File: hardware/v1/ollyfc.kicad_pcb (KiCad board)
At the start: 4 copper layers, 50 x 95 mm, 98 parts, among them J1 Conn_01x06, J10 Conn_01x03, J11 Conn_01x03, J13 Conn_01x05, J2 Conn_01x02, J3 Conn_01x03, J4 USB_C_Receptacle_USB2.0, J5 Conn_02x05_Odd_Even, J6 Conn_01x03, J7 Conn_01x03, J8 Conn_Coaxial, J9 Conn_01x03, Q1 AO3401A, Q2 MMBT3904, Q3 MMBT3904, Q4 MMBT3904, SW1 ACT/PASS, SW2 SW_Push, SW3 SW_Push, SW4 MODE1, SW5 MODE1, U1 AMS1117-3.3, U10 SRV05-4, U2 PCA9685BS, U3 STM32F411RETx, U4 LIS3MDL, U5 BMI088, U6 W25Q128JVS, U7 BMP388, U8 NEO-M8N, U9 TPS2113APW, Y1 X322516MLB4SI

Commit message: Route another?
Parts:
- removed R17: 5K1, Resistor_SMD:R_0402_1005Metric
- removed SW1: ACT/PASS, Button_Switch_SMD:SW_SPDT_PCM12
- added H6: MountingHole, MountingHole:MountingHole_3.2mm_M3, F.Cu at (15.2, 19.5)
- added J12: Conn_01x04, Connector_PinHeader_2.54mm:PinHeader_1x05_P2.54mm_Vertical, F.Cu at (-7.66, 16.8)
- added J14: Conn_01x04, Connector_PinHeader_2.54mm:PinHeader_1x04_P2.54mm_Vertical, F.Cu at (13.8, -14.7)
- added J15: Conn_01x04, Connector_PinHeader_2.54mm:PinHeader_1x04_P2.54mm_Vertical, F.Cu at (2.40, 20.8)
- added JP1: Jumper_2_Open, Connector_PinHeader_2.54mm:PinHeader_1x02_P2.54mm_Vertical, F.Cu at (9.25, -37.0)
- added R1: 5K1, Resistor_SMD:R_0402_1005Metric, F.Cu at (5.60, -17.2)
- J13: value Conn_01x05 -> Conn_01x04; footprint Connector_PinHeader_2.54mm:PinHeader_1x05_P2.54mm_Vertical -> Connector_PinHeader_2.54mm:PinHeader_1x04_P2.54mm_Vertical
- moved H1 99.0 mm to (15.2, -37.5)
- moved R12 83.5 mm to (11.5, -16.0), turned to 90 degrees
- moved H4 80.1 mm to (15.2, 50.0)
- moved BT1 71.4 mm to (-8.60, -23.8), turned to -90 degrees
- moved R6 68.0 mm to (18.2, -1.75), turned to 90 degrees
- moved R7 67.3 mm to (9.75, 7.00), turned to 90 degrees
- moved R10 64.3 mm to (18.2, 0.51), turned to -90 degrees
- moved SW5 63.5 mm to (18.1, -9.70), turned to 90 degrees
- moved D1 60.8 mm to (19.2, -3.75), turned to 180 degrees
- moved D3 58.1 mm to (19.2, 2.50), turned to 180 degrees
- moved J3 47.2 mm to (-17.2, 31.3), turned to 0 degrees
- moved H5 43.9 mm to (-15.2, 19.5)
- moved J6 42.0 mm to (-17.2, 37.0), turned to 0 degrees
- moved J13 40.3 mm to (-17.5, -8.79)
- moved R26 39.9 mm to (-0.99, 37.5)
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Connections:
- net SWDCLK renamed JTCK_SWCLK
- net SWDIO renamed JTMS_SWDIO
- net SWO renamed JTDO_SWO
- BZ1 pad N: (no net) -> Net-(BZ1-+)
- BZ1 pad P: (no net) -> 5VIN
- C26 pad 1: Net-(C26-Pad1) -> Net-(JP1-B)
- J5 pad 10: NRST -> JTRST
- J5 pad 8: unconnected-(J5-Pin_8-Pad8) -> JTDI
- L1 pad 1: Net-(C26-Pad1) -> Net-(JP1-A)
- Q3 pad 3: USART6_RX -> USART1_RX
- R12 pad 2: I2C3_SCL -> I2C1_SCL
- R19 pad 1: Net-(SW1-C) -> Net-(U8-VCC_RF)
- R19 pad 2: Net-(C26-Pad1) -> Net-(JP1-B)
- R2 pad 1: USART6_TX -> USART1_TX
- R5 pad 1: USART6_RX -> USART1_RX
- R8 pad 2: I2C2_SCL -> I2C2_SDA
- R9 pad 2: I2C2_SDA -> I2C2_SCL
- U2 pad 10: STATUS_B -> unconnected-(U2-LED7-Pad10)
- U2 pad 15: unconnected-(U2-LED11-Pad15) -> /IO/SERVO_CH4
- U2 pad 16: unconnected-(U2-LED12-Pad16) -> /IO/SERVO_CH5
- U2 pad 17: /IO/SERVO_CH4 -> /IO/SERVO_CH6
- U2 pad 18: /IO/SERVO_CH5 -> STATUS_A
- U2 pad 19: /IO/SERVO_CH6 -> STATUS_B
- U2 pad 23: I2C3_SCL -> I2C2_SCL
- U2 pad 24: I2C3_SDA -> I2C2_SDA
- U2 pad 9: STATUS_A -> unconnected-(U2-LED6-Pad9)
- U3 pad 10: SPI2_MOSI -> MODE1
- U3 pad 11: SPI2_MISO -> unconnected-(U3-PC3-Pad11)
- U3 pad 2: LED1 -> MAG_INT
- U3 pad 20: USART2_CK -> FMEM_CS
- U3 pad 21: PWR_STATE -> SPI1_SCK
- U3 pad 22: GYRO_INT3 -> SPI1_MISO
- U3 pad 23: CSB_GYRO -> SPI1_MOSI
- U3 pad 24: GYRO_INT4 -> unconnected-(U3-PC4-Pad24)
- U3 pad 25: CSB_ACCEL -> unconnected-(U3-PC5-Pad25)
- U3 pad 26: ACCEL_INT1 -> FMEM_HOLD
- U3 pad 27: GNSS_TIMEP -> PRES_INT
- U3 pad 28: GNSS_INT -> unconnected-(U3-PB2-Pad28)
- U3 pad 3: LED2 -> ACCEL_INT2
- U3 pad 34: SPI2_SCK -> unconnected-(U3-PB13-Pad34)
- U3 pad 35: MAG_CS -> LED2
- U3 pad 36: MAG_DRDY -> unconnected-(U3-PB15-Pad36)
- U3 pad 37: USART6_TX -> PWR_STATE
- U3 pad 38: USART6_RX -> LED1
- U3 pad 39: MAG_INT -> MODE2
- U3 pad 4: unconnected-(U3-PC15-Pad4) -> ACCEL_INT1
- U3 pad 40: I2C3_SDA -> unconnected-(U3-PC9-Pad40)
- U3 pad 41: I2C3_SCL -> unconnected-(U3-PA8-Pad41)
- U3 pad 42: BUZZER -> USART1_TX
- U3 pad 43: GNSS_CS -> USART1_RX
- U3 pad 50: FMEM_CS -> JTDI
- U3 pad 51: SPI1_SCK -> GNSS_TIMEP
- U3 pad 52: SPI1_MISO -> GNSS_INT
- U3 pad 53: SPI1_MOSI -> GNSS_RESET
- U3 pad 56: FMEM_HOLD -> JTRST
- U3 pad 57: unconnected-(U3-PB5-Pad57) -> GYRO_INT3
- U3 pad 58: MODE1 -> I2C1_SCL
- U3 pad 59: MODE2 -> I2C1_SDA
- U3 pad 61: ACCEL_INT2 -> GYRO_INT4
- U3 pad 8: PWR_STATE -> unconnected-(U3-PC0-Pad8)
- U3 pad 9: PRES_INT -> MAG_DRDY
- U4 pad 1: SPI2_SCK -> I2C1_SCL
- U4 pad 10: MAG_CS -> +3V3
- U4 pad 11: SPI2_MOSI -> I2C1_SDA
- U4 pad 9: SPI2_MISO -> GND
- U5 pad 10: SPI2_MISO -> GND
- U5 pad 14: CSB_ACCEL -> +3V3
- U5 pad 15: SPI2_MISO -> GND
- U5 pad 2: unconnected-(U5-NC-Pad2) -> GND
- U5 pad 5: CSB_GYRO -> unconnected-(U5-CSB2-Pad5)
- U5 pad 7: GND -> +3V3
- U5 pad 8: SPI2_SCK -> I2C1_SCL
- U5 pad 9: SPI2_MOSI -> I2C1_SDA
- U8 pad 14: LNA_EN -> unconnected-(U8-LNA_EN-Pad14)
- U8 pad 18: GNSS_CS -> I2C1_SDA
- U8 pad 19: SPI2_SCK -> I2C1_SCL
- U8 pad 2: GND -> unconnected-(U8-D_SEL-Pad2)
- U8 pad 20: SPI2_MISO -> unconnected-(U8-TXD/SPI_MISO-Pad20)
- U8 pad 21: SPI2_MOSI -> unconnected-(U8-RXD/SPI_MOSI-Pad21)
- U8 pad 9: Net-(SW1-B) -> Net-(U8-VCC_RF)
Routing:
- net SPI2_MISO: track 86.3 -> 0.00 mm, vias 6 -> 0
- net SPI2_MOSI: track 66.5 -> 0.00 mm, vias 3 -> 0
- net SPI2_SCK: track 65.2 -> 0.00 mm, vias 5 -> 0
- net I2C1_SDA: track 0.00 -> 64.0 mm, vias 0 -> 3
- net VBUS: track 74.9 -> 14.9 mm, vias 3 -> 6
- net I2C1_SCL: track 0.00 -> 57.7 mm, vias 0 -> 2
- net I2C2_SCL: track 7.13 -> 63.4 mm, vias 0 -> 2
- net USART2_CK: track 48.4 -> 0.00 mm, vias 1 -> 0
- net VIN_EXT: track 43.0 -> 0.00 mm
- net VBAT: track 3.54 -> 43.0 mm, vias 0 -> 2
- net MAG_CS: track 35.3 -> 0.00 mm, vias 4 -> 0
- net I2C2_SDA: track 27.6 -> 62.6 mm, vias 2 -> 1
- net Net-(D4-A): track 35.8 -> 1.62 mm, vias 2 -> 0
- net GNSS_RESET: track 1.60 -> 34.4 mm, vias 1 -> 2
- net USART1_RX: track 0.00 -> 31.9 mm
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- added copper zone on In2.Cu, net +3V3
- added copper zone on In2.Cu, net VBUS
- added copper zone on F.Cu, net VIN_EXT
- removed copper zone on F.Cu, net VIN
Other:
- board size 50 x 95 mm -> 42.5 x 99.5 mm
- board text added: "EXT ANT."
- board text added: "I2C1"
- board text removed: "P A"

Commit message: v2 PCB design
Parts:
- removed BT1: Battery_Cell, Battery:BatteryHolder_Keystone_3002_1x2032
- removed H6: MountingHole, MountingHole:MountingHole_3.2mm_M3
- removed J15: Conn_01x04, Connector_PinHeader_2.54mm:PinHeader_1x04_P2.54mm_Vertical
- BZ1: moved to B.Cu
- J13: footprint Connector_PinHeader_2.54mm:PinHeader_1x04_P2.54mm_Vertical -> Connector_PinHeader_2.54mm:PinHeader_1x08_P2.54mm_Vertical
- moved SW4 37.3 mm to (16.5, -29.0), turned to 90 degrees
- moved D4 36.8 mm to (-9.11, 21.2), turned to 0 degrees
- moved C15 35.2 mm to (-8.25, -20.5), turned to 90 degrees
- moved R8 34.7 mm to (2.75, -10.5), turned to -90 degrees
- moved D2 34.7 mm to (-3.00, 51.2), turned to 0 degrees
- moved U7 34.0 mm to (-6.24, -20.8), turned to 90 degrees
- moved R13 33.2 mm to (-5.86, 21.2), turned to 180 degrees
- moved C14 32.1 mm to (-7.25, -18.5), turned to 0 degrees
- moved R16 31.8 mm to (-2.75, 49.8), turned to 180 degrees
- moved J4 30.6 mm to (16.1, 40.9)
- moved H1 30.5 mm to (-15.2, -37.5)
- moved H2 30.5 mm to (15.2, -37.5)
- moved H5 30.5 mm to (15.2, 19.5)
- moved R7 30.4 mm to (9.25, 37.4)
- moved SW3 29.3 mm to (11.5, 9.75), turned to 0 degrees
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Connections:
- J13 pad 1: USART2_CTS -> GND
- J13 pad 2: USART2_RTS -> +3V3
- J13 pad 3: USART2_TX -> I2C2_SCL
- J13 pad 4: USART2_RX -> I2C2_SDA
- U3 pad 10: MODE1 -> unconnected-(U3-PC2-Pad10)
- U3 pad 2: MAG_INT -> unconnected-(U3-PC13-Pad2)
- U3 pad 24: unconnected-(U3-PC4-Pad24) -> MAG_INT
- U3 pad 27: PRES_INT -> MODE1
- U3 pad 28: unconnected-(U3-PB2-Pad28) -> MODE2
- U3 pad 3: ACCEL_INT2 -> ACCEL_INT1
- U3 pad 36: unconnected-(U3-PB15-Pad36) -> BUZZER
- U3 pad 39: MODE2 -> unconnected-(U3-PC8-Pad39)
- U3 pad 4: ACCEL_INT1 -> ACCEL_INT2
- U3 pad 41: unconnected-(U3-PA8-Pad41) -> GNSS_SAFEBOOT
- U3 pad 51: GNSS_TIMEP -> GNSS_RESET
- U3 pad 53: GNSS_RESET -> GNSS_TIMEP
- U3 pad 8: unconnected-(U3-PC0-Pad8) -> MAG_DRDY
- U3 pad 9: MAG_DRDY -> PRES_INT
- U7 pad 2: I2C2_SCL -> I2C1_SCL
- U7 pad 4: I2C2_SDA -> I2C1_SDA
- U8 pad 18: I2C1_SDA -> I2C2_SDA
- U8 pad 19: I2C1_SCL -> I2C2_SCL
- U8 pad 22: VBAT -> +3V3
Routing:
- net VIN_EXT: track 0.00 -> 49.3 mm
- net GNSS_SAFEBOOT: track 0.00 -> 47.3 mm, vias 0 -> 2
- net VBAT: track 43.0 -> 0.00 mm, vias 2 -> 0
- net GND: track 122.3 -> 156.2 mm, vias 86 -> 79
- net VBUS: track 14.9 -> 43.8 mm, vias 6 -> 5
- net I2C2_SDA: track 62.6 -> 90.1 mm, vias 1 -> 4
- net USART1_RX: track 31.9 -> 4.68 mm
- net /SBUS_OUT: track 10.3 -> 37.1 mm
- net I2C2_SCL: track 63.4 -> 88.7 mm, vias 2 -> 4
- net USBD-: track 22.0 -> 46.9 mm
- net /S_PORT: track 13.8 -> 37.6 mm
- net USBD+: track 22.1 -> 45.5 mm
- net I2C1_SDA: track 64.0 -> 41.9 mm, vias 3 -> 0
- net PWR_STATE: track 27.8 -> 49.4 mm, vias 2 -> 0
- net MODE1: track 24.6 -> 46.1 mm
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- added copper zone on F.Cu, net VIN
- removed copper zone on F.Cu, net 5VIN
- removed copper zone on In2.Cu, net VBUS
- removed copper zone on F.Cu, net VIN_EXT
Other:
- board size 42.5 x 99.5 mm -> 40.5 x 97.5 mm
- board text added: "SPI1"
- board text added: "ch1"
- board text added: "ch2"
- board text added: "ch3"
- board text added: "ch4"
- board text added: "ch5"
- board text added: "ch6"
- board text removed: "EXT ANT."
- board text removed: "I2C1"

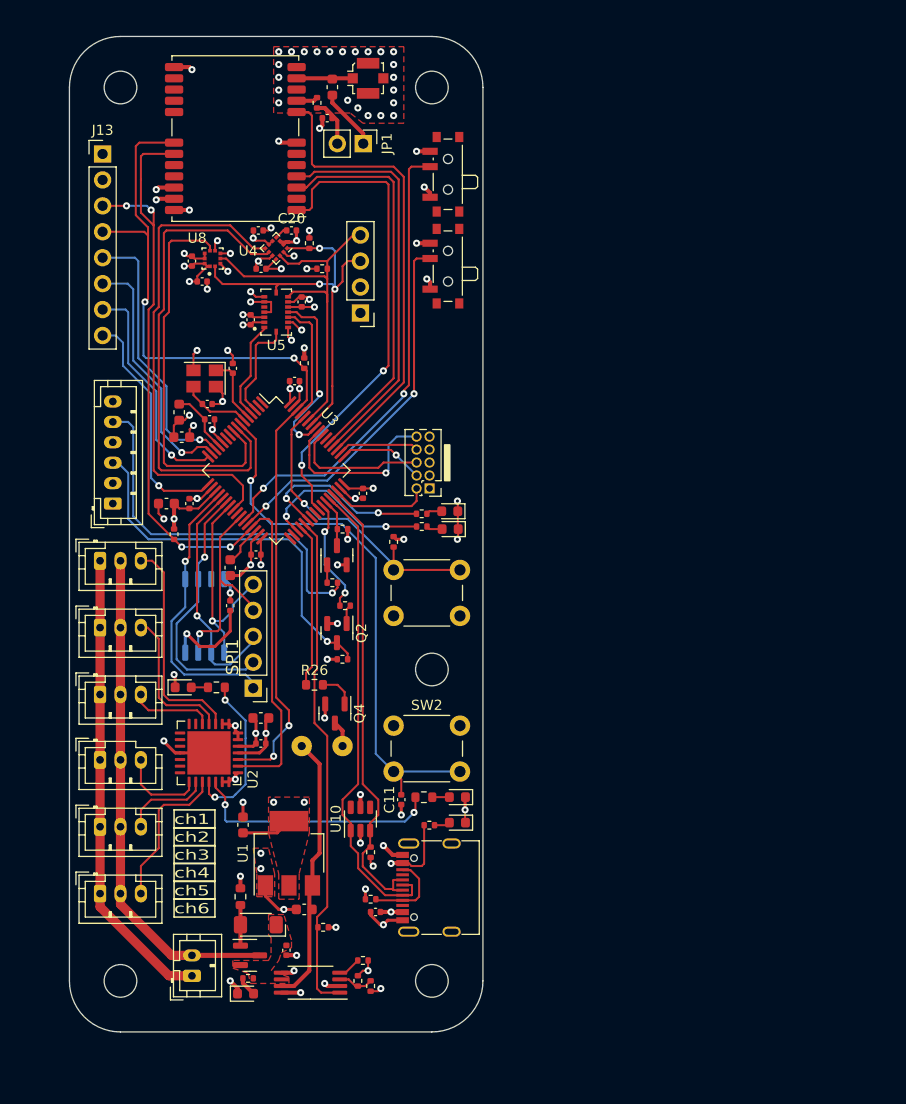
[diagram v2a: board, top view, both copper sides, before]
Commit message: JLC part footprints
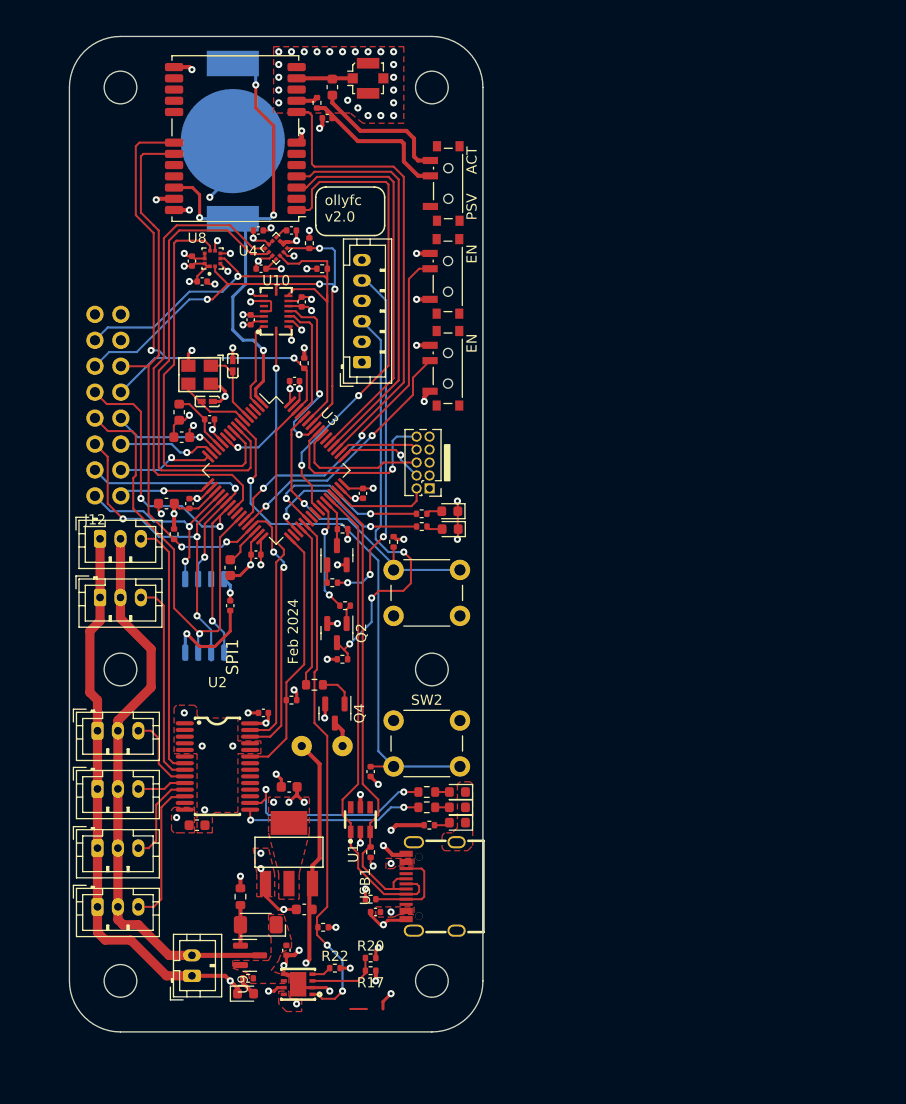
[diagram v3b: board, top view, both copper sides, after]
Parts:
- removed J14: Conn_01x04, Connector_PinHeader_2.54mm:PinHeader_1x04_P2.54mm_Vertical
- removed J4: USB_C_Receptacle_USB2.0, Connector_USB:USB_C_Receptacle_G-Switch_GT-USB-7010ASV
- removed JP1: Jumper_2_Open, Connector_PinHeader_2.54mm:PinHeader_1x02_P2.54mm_Vertical
- removed R24: 1K5, Resistor_SMD:R_0402_1005Metric
- removed U5: BMI088, ollyfc:PQFN50P450X300X100-16N
- removed Y1: X322516MLB4SI, Crystal:Crystal_SMD_SeikoEpson_TSX3225-4Pin_3.2x2.5mm
- added BT1: Battery_Cell, Battery:BatteryHolder_LINX_BAT-HLD-012-SMT, B.Cu at (-4.25, -32.2)
- added D8: SRV05-4_C7420376, ofc_sym:SOT-23-6_L2.9-W1.6-P0.95-LS2.8-BL-1, F.Cu at (8.25, 34.2)
- added H6: MountingHole, MountingHole:MountingHole_3.2mm_M3, F.Cu at (-15.2, 19.5)
- added R17: 1K5, Resistor_SMD:R_0402_1005Metric, F.Cu at (9.25, 49.0)
- added R20: 1K5, Resistor_SMD:R_0402_1005Metric, F.Cu at (9.25, 47.8)
- added SW6: MODE1, Button_Switch_SMD:SW_SPDT_PCM12, F.Cu at (16.5, -28.1)
- added USB1: USB-TYPE-C-018, ofc_sym:USB-C_SMD-TYPE-C-31-M-12, F.Cu at (15.2, 40.8)
- added X1: X322516MLB4SI, ofc_sym:OSC-SMD_4P-L3.2-W2.5-BL, F.Cu at (-7.50, -9.37)
- C10, C9: value 10pF -> 12pF; footprint Capacitor_SMD:C_0402_1005Metric -> ofc_sym:C0402
- J12: value Conn_01x04 -> Conn_01x08; footprint Connector_PinHeader_2.54mm:PinHeader_1x05_P2.54mm_Vertical -> Connector_PinHeader_2.54mm:PinHeader_1x08_P2.54mm_Vertical
- R23: value 1K5 -> 5K1
- U1: footprint Package_TO_SOT_SMD:SOT-223-3_TabPin2 -> ofc_sym:SOT-223-3_L6.5-W3.4-P2.30-LS7.0-BR
- U10: value SRV05-4 -> BMI088; footprint Package_TO_SOT_SMD:SOT-23-6 -> ofc_sym:LGA-16_L4.5-W3.0-P0.50-BL
- U2: value PCA9685BS -> PCA9685PW,118; footprint Package_DFN_QFN:QFN-28-1EP_6x6mm_P0.65mm_EP4.25x4.25mm -> ofc_sym:TSSOP-28_L9.7-W4.4-P0.65-LS6.4-TL
- U9: value TPS2113APW -> TPS2113ADRBR; footprint Package_SO:TSSOP-8_4.4x3mm_P0.65mm -> ofc_sym:SON-8_L3.0-W3.0-P0.65-LS3.0-BL-EP
- moved U10 50.4 mm to (0.00, -15.6), turned to 0 degrees
- moved D4 29.3 mm to (17.8, 33.0), turned to 180 degrees
- moved R23 29.1 mm to (1.50, 22.5), turned to 0 degrees
- moved J1 28.1 mm to (8.40, -10.6)
- moved J12 24.4 mm to (-17.8, 2.50)
- moved R13 23.7 mm to (14.8, 33.0), turned to 0 degrees
- moved J13 15.8 mm to (-15.2, -15.3)
- moved C18 12.2 mm to (-7.75, 34.8), turned to 0 degrees
- moved SW4 10.0 mm to (16.5, -19.0)
- moved SW5 10.0 mm to (16.5, -10.0)
- moved C19 5.86 mm to (1.27, 31.0), turned to 180 degrees
- moved C11 4.07 mm to (9.25, 29.5)
- moved J7 3.56 mm to (-17.5, 25.5)
- moved C17 3.01 mm to (-1.25, 23.8)
- moved J6 2.95 mm to (-17.3, 12.4)
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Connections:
- J13 pad 1: GND -> +3V3
- J13 pad 2: +3V3 -> unconnected-(J13-Pin_2-Pad2)
- R21 pad 1: Net-(J4-CC1) -> USBCC
- R23 pad 1: VBUS -> PWM_EN
- R23 pad 2: /Power/VSNS -> GND
- U10 pad 1: USBD- -> ACCEL_INT2
- U10 pad 3: USBD+ -> +3V3
- U10 pad 4: unconnected-(U10-IO3-Pad4) -> GND
- U10 pad 5: VBUS -> unconnected-(U10-CSB2-Pad5)
- U10 pad 6: unconnected-(U10-IO4-Pad6) -> GND
- U2 pad 10: unconnected-(U2-LED7-Pad10) -> /IO/SERVO_CH4
- U2 pad 11: GND -> /IO/SERVO_CH5
- U2 pad 12: unconnected-(U2-LED8-Pad12) -> /IO/SERVO_CH6
- U2 pad 14: unconnected-(U2-LED10-Pad14) -> +3V3
- U2 pad 15: /IO/SERVO_CH4 -> STATUS_A
- U2 pad 16: /IO/SERVO_CH5 -> STATUS_B
- U2 pad 17: /IO/SERVO_CH6 -> unconnected-(U2-LED10-Pad17)
- U2 pad 18: STATUS_A -> unconnected-(U2-LED11-Pad18)
- U2 pad 19: STATUS_B -> unconnected-(U2-LED12-Pad19)
- U2 pad 20: GND -> unconnected-(U2-LED13-Pad20)
- U2 pad 21: GND -> unconnected-(U2-LED14-Pad21)
- U2 pad 22: GND -> unconnected-(U2-LED15-Pad22)
- U2 pad 23: I2C2_SCL -> PWM_EN
- U2 pad 24: I2C2_SDA -> GND
- U2 pad 25: +3V3 -> GND
- U2 pad 26: GND -> I2C2_SCL
- U2 pad 27: GND -> I2C2_SDA
- U2 pad 28: GND -> +3V3
- U2 pad 3: /IO/SERVO_CH1 -> GND
- U2 pad 4: /IO/SERVO_CH2 -> GND
- U2 pad 5: /IO/SERVO_CH3 -> GND
- U2 pad 7: unconnected-(U2-LED4-Pad7) -> /IO/SERVO_CH1
- U2 pad 8: unconnected-(U2-LED5-Pad8) -> /IO/SERVO_CH2
- U2 pad 9: unconnected-(U2-LED6-Pad9) -> /IO/SERVO_CH3
- U3 pad 11: unconnected-(U3-PC3-Pad11) -> ACCEL_INT1
- U3 pad 2: unconnected-(U3-PC13-Pad2) -> ACCEL_INT2
- U3 pad 3: ACCEL_INT1 -> unconnected-(U3-PC14-Pad3)
- U3 pad 33: unconnected-(U3-PB12-Pad33) -> PWM_EN
- U3 pad 4: ACCEL_INT2 -> unconnected-(U3-PC15-Pad4)
- U8 pad 22: +3V3 -> VBAT
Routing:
- net VBAT: track 0.00 -> 51.1 mm, vias 0 -> 4
- net PWM_EN: track 0.00 -> 25.2 mm
- net FMEM_HOLD: track 20.6 -> 42.9 mm
- net SPI1_MOSI: track 21.4 -> 39.3 mm, vias 1 -> 3
- net USART2_CTS: track 26.9 -> 10.6 mm
- net USART2_RTS: track 24.6 -> 9.70 mm
- net USART2_RX: track 23.1 -> 9.02 mm
- net I2C1_SDA: track 41.9 -> 55.0 mm, vias 0 -> 1
- net USART2_TX: track 22.3 -> 9.30 mm
- net I2C1_SCL: track 42.3 -> 53.7 mm, vias 3 -> 4
- net MODE2: track 36.2 -> 25.5 mm
- net SPI1_SCK: track 23.2 -> 33.9 mm, vias 1 -> 3
- net MODE1: track 46.1 -> 35.6 mm
- net Net-(SW6-B): track 5.78 -> 15.9 mm
- net USBCC: track 0.00 -> 9.38 mm
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- added copper zone on F.Cu, net VBUS
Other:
- board text added: "ACT"
- board text added: "EN"
- board text added: "Feb 2024"
- board text added: "PSV"
- board text added: "ollyfc v2.0"
- board text removed: "ch1"
- board text removed: "ch2"
- board text removed: "ch3"
- board text removed: "ch4"
- board text removed: "ch5"
- board text removed: "ch6"
